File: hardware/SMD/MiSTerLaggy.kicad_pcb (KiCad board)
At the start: 2 copper layers, 19.8 x 12.5 mm, 9 parts, among them J1 USB_C_Receptacle_USB2.0, Q1 Q_Photo_NPN

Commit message: New circuit design
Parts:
- removed H3, H4: MountingHole_Pad, MountingHole:MountingHole_2.2mm_M2_ISO7380
- removed the R1 at (134.4, 73.4)
- removed R2: ??, Resistor_SMD:R_0603_1608Metric
- J1: footprint Connector_USB:USB_C_Receptacle_G-Switch_GT-USB-7010ASV -> Connector_USB:USB_C_Receptacle_GCT_USB4085
- Q1: value Q_Photo_NPN -> PT17-21C/L41/TR8; footprint LED_SMD:LED_0805_2012Metric -> LED_THT:LED_D3.0mm
- R1: renamed from R3; value ?? -> 750K; footprint Resistor_SMD:R_0603_1608Metric -> Resistor_THT:R_Axial_DIN0207_L6.3mm_D2.5mm_P7.62mm_Horizontal
- moved H2 11.9 mm to (131.1, 80.4)
- moved H1 11.9 mm to (124.3, 80.4)
- moved R1 7.85 mm to (131.5, 76.3), turned to 180 degrees
- moved J1 3.78 mm to (130.7, 73.6)
- moved Q1 0.90 mm to (127.7, 79.1), turned to -90 degrees
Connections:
- net Net-(J1-D--PadA7) renamed +3.3V
- J1 pad A4: +5V -> unconnected-(J1-VBUS-PadA4)
- J1 pad A6: Net-(J1-D+-PadA6) -> Net-(Q1-C)
- J1 pad A9: +5V -> unconnected-(J1-VBUS-PadA4)
- J1 pad B4: +5V -> unconnected-(J1-VBUS-PadA4)
- J1 pad B6: Net-(J1-D+-PadA6) -> Net-(Q1-C)
- J1 pad B9: +5V -> unconnected-(J1-VBUS-PadA4)
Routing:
- net Net-(J1-D+-PadA6): track 10.5 -> 0.00 mm, vias 2 -> 0
- net +5V: track 10.1 -> 0.00 mm
- net Net-(Q1-C): track 3.14 -> 11.4 mm
- net unconnected-(J1-VBUS-PadA4): track 0.00 -> 8.09 mm
- net +3.3V: track 11.2 -> 6.49 mm
- net GND: track 6.60 -> 2.70 mm, vias 1 -> 0
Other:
- board size 19.8 x 12.5 mm -> 11 x 15.4 mm
- board text added: "@wickerwaka"
- board text added: "JLCJLCJLCJLC"
- board text added: "MrLaggy"
- board text added: "v1.0"

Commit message: MOSFET usage
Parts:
- added Q2: 2N7002, Package_TO_SOT_SMD:SOT-23, F.Cu at (124.4, 79.1)
- J1: footprint Connector_USB:USB_C_Receptacle_GCT_USB4085 -> Connector_USB:USB_C_Receptacle_G-Switch_GT-USB-7010ASV
- Q1: footprint LED_THT:LED_D3.0mm -> LED_SMD:LED_0805_2012Metric
- R1: footprint Resistor_THT:R_Axial_DIN0207_L6.3mm_D2.5mm_P7.62mm_Horizontal -> Resistor_SMD:R_0805_2012Metric
- moved J1 3.26 mm to (127.7, 72.3)
- moved R1 2.85 mm to (131.0, 79.1), turned to 90 degrees
- moved Q1 2.80 mm to (127.7, 81.9)
- moved H1 2.71 mm to (124.5, 83.1)
- moved H2 2.71 mm to (130.9, 83.1)
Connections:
- J1 pad A4: unconnected-(J1-VBUS-PadA4) -> Net-(J1-VBUS-PadA4)
- J1 pad A6: Net-(Q1-C) -> unconnected-(J1-D+-PadA6)
- J1 pad A7: +3.3V -> Net-(Q2-D)
- J1 pad A9: unconnected-(J1-VBUS-PadA4) -> Net-(J1-VBUS-PadA4)
- J1 pad B4: unconnected-(J1-VBUS-PadA4) -> Net-(J1-VBUS-PadA4)
- J1 pad B6: Net-(Q1-C) -> unconnected-(J1-D+-PadB6)
- J1 pad B7: +3.3V -> Net-(Q2-D)
- J1 pad B9: unconnected-(J1-VBUS-PadA4) -> Net-(J1-VBUS-PadA4)
- R1 pad 2: +3.3V -> Net-(J1-VBUS-PadA4)
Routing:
- net Net-(J1-VBUS-PadA4): track 0.00 -> 8.99 mm
- net unconnected-(J1-VBUS-PadA4): track 8.09 -> 0.00 mm
- net +3.3V: track 6.49 -> 0.00 mm
- net Net-(Q2-D): track 0.00 -> 6.03 mm
- net GND: track 2.70 -> 4.93 mm, vias 0 -> 2
- net Net-(Q1-C): track 11.4 -> 9.42 mm
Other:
- board size 11 x 15.4 mm -> 10.6 x 17.1 mm
- board text added: "C"
- board text added: "E"

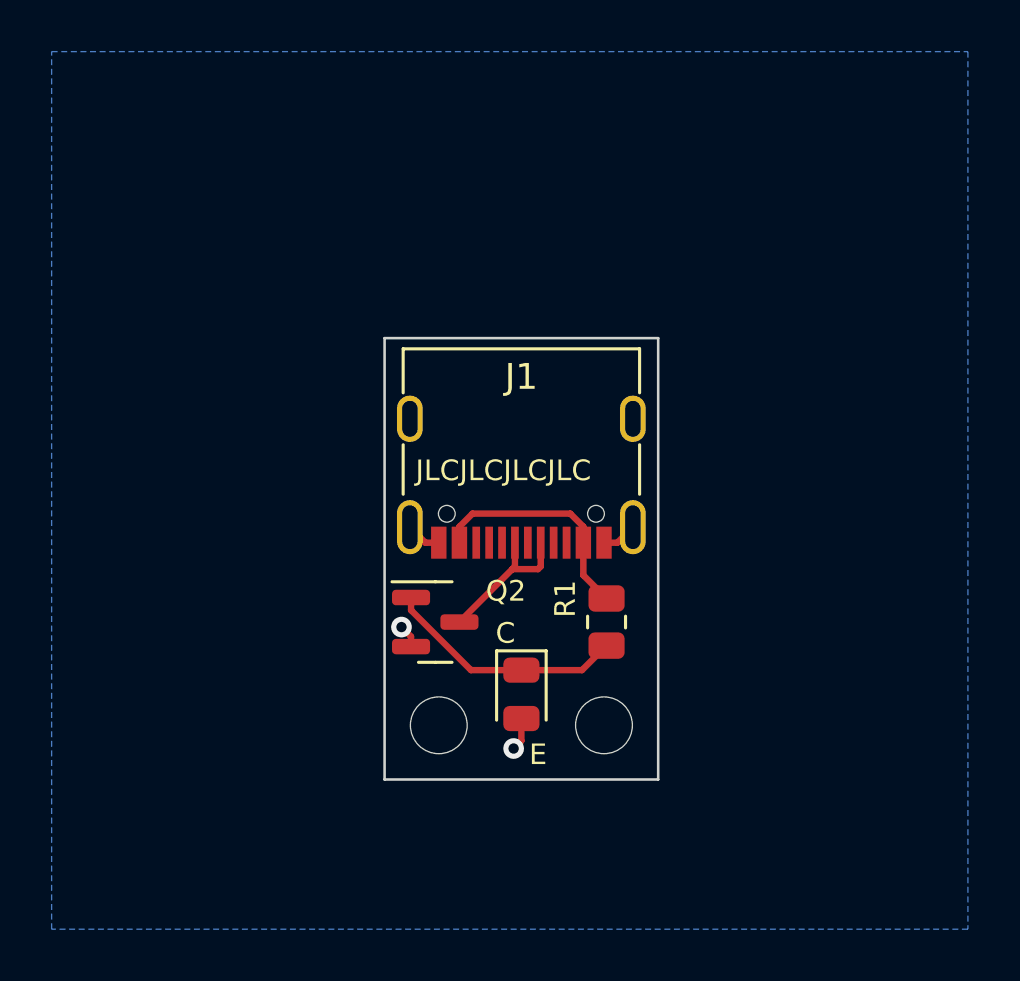
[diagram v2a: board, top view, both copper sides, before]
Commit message: Add pulldown
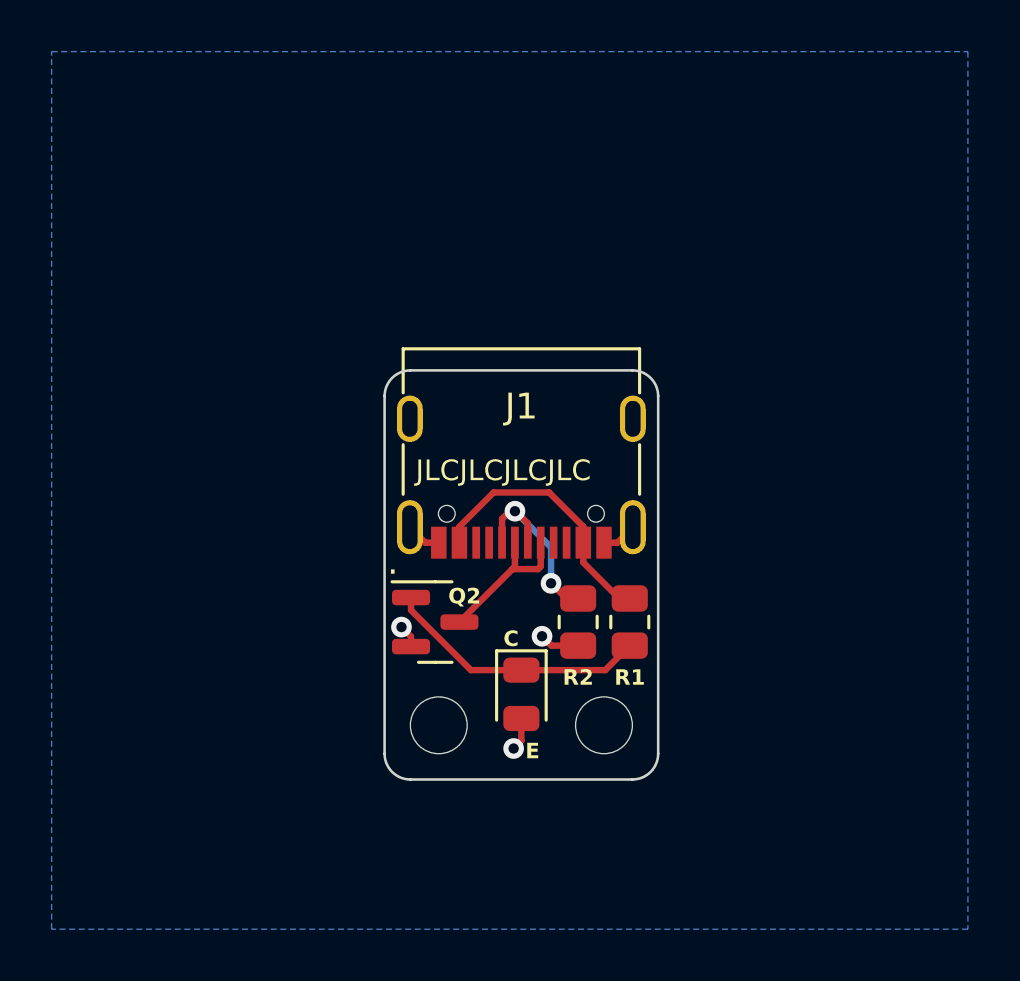
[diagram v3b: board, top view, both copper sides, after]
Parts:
- added R2: 1K, Resistor_SMD:R_0805_2012Metric, F.Cu at (129.9, 79.1)
- moved R1 0.90 mm to (131.9, 79.1)
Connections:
- net Net-(J1-VBUS-PadA4) renamed VBUS
- J1 pad A6: unconnected-(J1-D+-PadA6) -> Net-(J1-D+-PadA6)
- J1 pad B6: unconnected-(J1-D+-PadB6) -> Net-(J1-D+-PadA6)
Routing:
- net Net-(J1-D+-PadA6): track 0.00 -> 7.65 mm, vias 0 -> 2
- net GND: track 4.93 -> 6.48 mm, vias 2 -> 3
- net VBUS: track 8.99 -> 10.3 mm
- net Net-(Q1-C): track 9.42 -> 10.3 mm
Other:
- board size 10.6 x 17.1 mm -> 10.6 x 15.9 mm
- board text added: "."
- board text added: "v1.1"
- board text removed: "v1.0"
